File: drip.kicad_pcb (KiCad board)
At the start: 2 copper layers, 82 parts, among them J1 ISP, J2 2xAA Battery Holder, Q1 2n2907, Q2 2n2907, Q3 2n2907, Q4 2n2907, Q5 2n2907, Q6 2n2907, Q7 2n2907, Q8 2n2907, Q9 2n2222, SW1 Bin, SW10 Recall, SW11 D, SW12 A, SW13 7, SW14 4, SW15 1, SW16 0, SW17 Hex, SW18 E, SW19 B, SW2 Store, SW20 8, SW21 5, SW22 2, SW23 Decimal, SW24 Oct, SW25 F, SW26 C, SW27 9, SW28 6, SW29 3, SW3 Shift, SW30 +/-, SW31 Clear, SW32 K, SW33 Div, SW34 Mul, SW35 Minus, SW36 Plus, SW37 Enter, SW4 1'sCompl, SW5 Or, SW6 And, SW7 Xor, SW8 Clear Entry, SW9 Dec, U1 74HC138, U2 5641AS-4Digit-7Segment, U3 5641AS-4Digit-7Segment, U4 MSP430G2553IN20, U5 74HC251, U6 74HC138, U7 74HC595

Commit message: Step-up converter, layout of keypad
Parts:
- added C1: 220µF, Capacitor_THT:CP_Radial_D8.0mm_P5.00mm, F.Cu at (28.7, 159.7)
- added C2: 47µF, Capacitor_Tantalum_SMD:CP_EIA-3528-15_AVX-H_Pad1.50x2.35mm_HandSolder, F.Cu at (39.1, 158.9)
- added D2: 1n5817, Diode_THT:D_DO-41_SOD81_P10.16mm_Horizontal, F.Cu at (28.1, 152.8)
- added L1: 100µH, Inductor_SMD:L_0805_2012Metric_Pad1.15x1.40mm_HandSolder, F.Cu at (38.3, 162.6)
- added U8: XC6372A331PR-G, Package_TO_SOT_SMD:SOT-89-3_Handsoldering, F.Cu at (44.2, 153.7)
- moved SW2 168.1 mm to (168.8, 131.9)
- moved SW8 158.7 mm to (168.8, 192.8)
- moved SW1 151.3 mm to (168.8, 122.0)
- moved SW6 151.3 mm to (168.8, 172.5)
- moved SW17 148.7 mm to (190.1, 122.0)
- moved SW27 148.6 mm to (200.7, 162.3)
- moved SW26 144.4 mm to (200.7, 152.2)
- moved SW14 143.5 mm to (179.4, 172.5)
- moved SW10 141.2 mm to (179.4, 131.9)
- moved SW22 137.7 mm to (190.1, 182.7)
- moved SW7 130.2 mm to (168.8, 182.7)
- moved SW21 129.9 mm to (190.1, 172.5)
- moved SW4 125.5 mm to (168.8, 152.2)
- moved SW3 124.3 mm to (168.8, 142.0)
- moved SW19 123.7 mm to (190.1, 152.2)
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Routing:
- net /~{KBD_COL_0}: track 0.00 -> 141.1 mm
- net /~{KBD_COL_1}: track 0.00 -> 141.1 mm
- net /~{KBD_COL_3}: track 0.00 -> 132.2 mm
- net /~{KBD_COL_2}: track 0.00 -> 132.2 mm
- net /~{KBD_COL_4}: track 0.00 -> 132.2 mm
- net /KBD_ROW_0: track 0.00 -> 127.8 mm, vias 0 -> 2
- net /KBD_ROW_2: track 0.00 -> 102.4 mm, vias 0 -> 2
- net /KBD_ROW_3: track 0.00 -> 88.4 mm, vias 0 -> 2
- net /KBD_ROW_1: track 0.00 -> 83.1 mm, vias 0 -> 2
- net /KBD_ROW_4: track 0.00 -> 74.0 mm, vias 0 -> 2
- net /KBD_ROW_7: track 0.00 -> 66.8 mm, vias 0 -> 2
- net /KBD_ROW_5: track 0.00 -> 66.8 mm, vias 0 -> 2
- net /KBD_ROW_6: track 0.00 -> 59.1 mm
- net Net-(JP1-Pad2): track 13.0 -> 1.89 mm
- net Net-(JP2-Pad2): track 13.0 -> 2.25 mm
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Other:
- board outline added: 102.2 x 107.9 mm

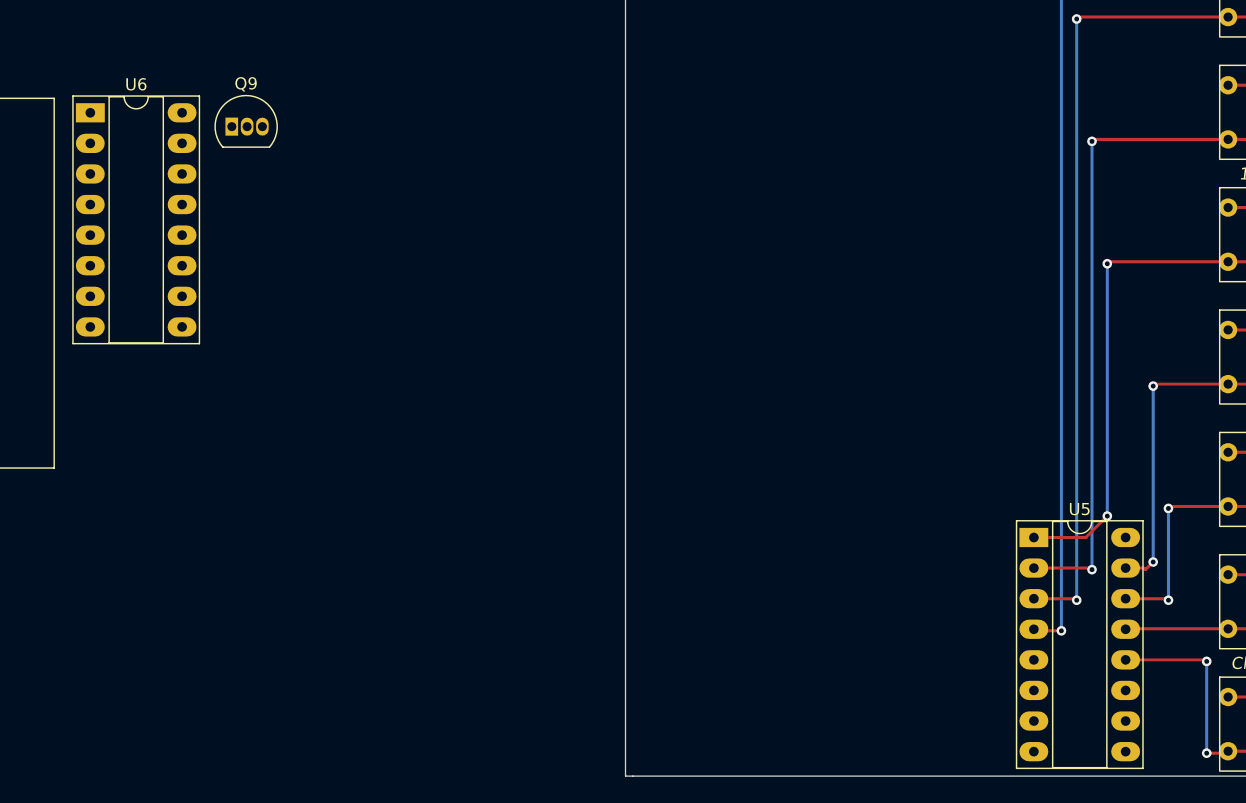
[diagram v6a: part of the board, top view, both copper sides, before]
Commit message: Minor PCB fettling
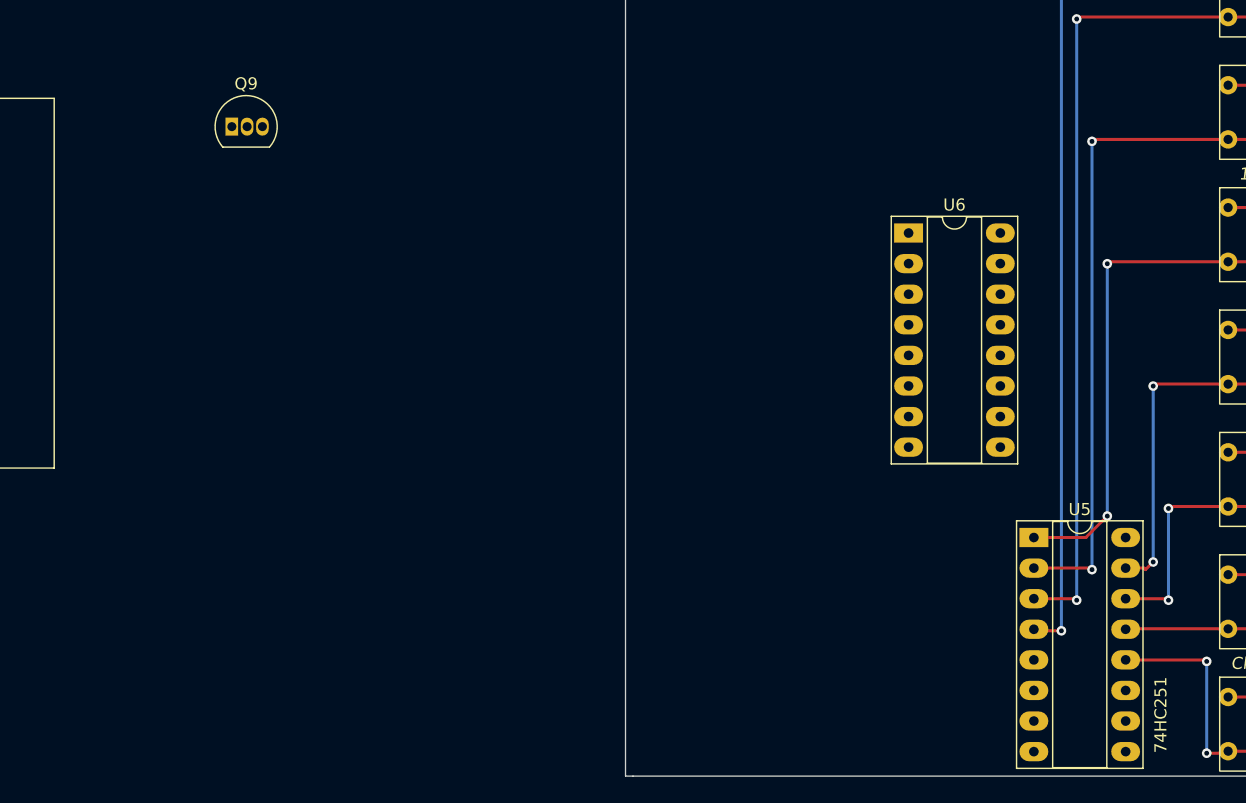
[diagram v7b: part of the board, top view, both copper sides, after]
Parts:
- moved U6 68.7 mm to (142.2, 154.3)
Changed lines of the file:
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@@
   )
   (footprint "Package_DIP:DIP-16_W7.62mm_Socket_LongPads" (layer "F.Cu")
-    (at 74.305 144.31)
+    (at 142.25 154.295)
     (descr "16-lead though-hole mounted DIP package, row spacing 7.62 mm (300 mils), Socket, LongPads")
     (tags "THT DIP DIL PDIP 2.54mm 7.62mm 300mil Socket LongPads")
@@
       (effects (font (size 1 1) (thickness 0.15)))
     )
-    (fp_text value "74HC251" (at 3.81 20.11) (layer "F.Fab")
-      (effects (font (size 1 1) (thickness 0.15)))
-    )
+    (fp_text value "74HC251" (at 10.541 14.732 90) (layer "F.SilkS")
+      (effects (font (size 1 1) (thickness 0.15)))
+    )

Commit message: All placed, kind of
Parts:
- removed the G*** at (198.1, 30.5)
- added G***: LOGO, Logos:little-drip-tiny, F.Cu at (203.8, 134.0)
- added REF**: MountingHole_3.2mm_M3_DIN965, MountingHole:MountingHole_3.2mm_M3_DIN965, F.Cu at (225.4, 101.0)
- moved R10 168.6 mm to (124.5, 132.1), turned to -90 degrees
- moved J1 164.1 mm to (121.9, 196.8), turned to 90 degrees
- moved U4 149.8 mm to (122.6, 189.9)
- moved R7 144.6 mm to (135.3, 144.1), turned to 90 degrees
- moved R3 142.3 mm to (150.5, 144.1), turned to 90 degrees
- moved R6 140.4 mm to (139.1, 144.1), turned to 90 degrees
- moved R8 138.8 mm to (131.4, 144.1), turned to 90 degrees
- moved JP1 138.6 mm to (124.5, 160.0), turned to 0 degrees
- moved R15 136.0 mm to (135.3, 131.4), turned to 90 degrees
- moved R17 133.2 mm to (146.7, 131.4), turned to 90 degrees
- moved JP2 130.6 mm to (124.5, 151.8), turned to 0 degrees
- moved U7 128.8 mm to (129.5, 171.4), turned to 90 degrees
- moved R18 128.1 mm to (154.3, 131.4), turned to 90 degrees
- moved R16 127.2 mm to (131.4, 131.4), turned to 90 degrees
- moved JP3 126.6 mm to (124.5, 148.9), turned to 0 degrees
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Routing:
- net GND: track 0.00 -> 231.9 mm, vias 0 -> 8
- net VCC: track 0.00 -> 212.3 mm, vias 0 -> 10
- net Net-(U2-Pad11): track 0.00 -> 107.3 mm, vias 0 -> 2
- net Net-(U2-Pad10): track 0.00 -> 96.7 mm, vias 0 -> 2
- net /KBD_DATA: track 0.00 -> 96.1 mm, vias 0 -> 1
- net /~{KBD_ROW_SEL_B}: track 0.00 -> 95.1 mm, vias 0 -> 4
- net /~{KBD_ROW_SEL_A}: track 0.00 -> 92.6 mm, vias 0 -> 3
- net Net-(U2-Pad3): track 0.00 -> 89.7 mm, vias 0 -> 3
- net /~{LED}/KBD: track 0.00 -> 88.8 mm, vias 0 -> 4
- net /SEL_1: track 0.00 -> 85.2 mm, vias 0 -> 3
- net Net-(U2-Pad2): track 0.00 -> 84.1 mm, vias 0 -> 3
- net Net-(U2-Pad7): track 0.00 -> 83.2 mm
- net /SEL_0: track 0.00 -> 82.9 mm, vias 0 -> 1
- net /SEL_2: track 0.00 -> 81.7 mm, vias 0 -> 4
- net Net-(U2-Pad5): track 0.00 -> 76.8 mm, vias 0 -> 2
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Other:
- board size 102.2 x 107.9 mm -> 119.4 x 107.9 mm
- board text added: "0"
- board text added: "1"
- board text added: "2"
- board text added: "3.3v"
- board text added: "4"
- board text added: "5"
- board text added: "6"
- board text added: "7"
- board text added: "Column Decode"
- board text added: "GND"
- board text added: "ND"
- board text added: "Out"
- board text added: "Row"
- board text added: "Row Decode"
- board text added: "Test"
- board text added: "leadedsolder.com 2023, v1"
- board text added: "s0"
- board text added: "s1"
- board text added: "s2"
- board text added: "~{0}"
- board text added: "~{1}"
- board text added: "~{2}"
- board text added: "~{3}"
- board text added: "~{4}"
- board text added: "~{KBD}"
- board text added: "~{RST}"
- board text removed: "leadedsolder.com 2023"
